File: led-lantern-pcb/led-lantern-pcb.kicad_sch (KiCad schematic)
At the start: 1 part, among them U1 TP4056

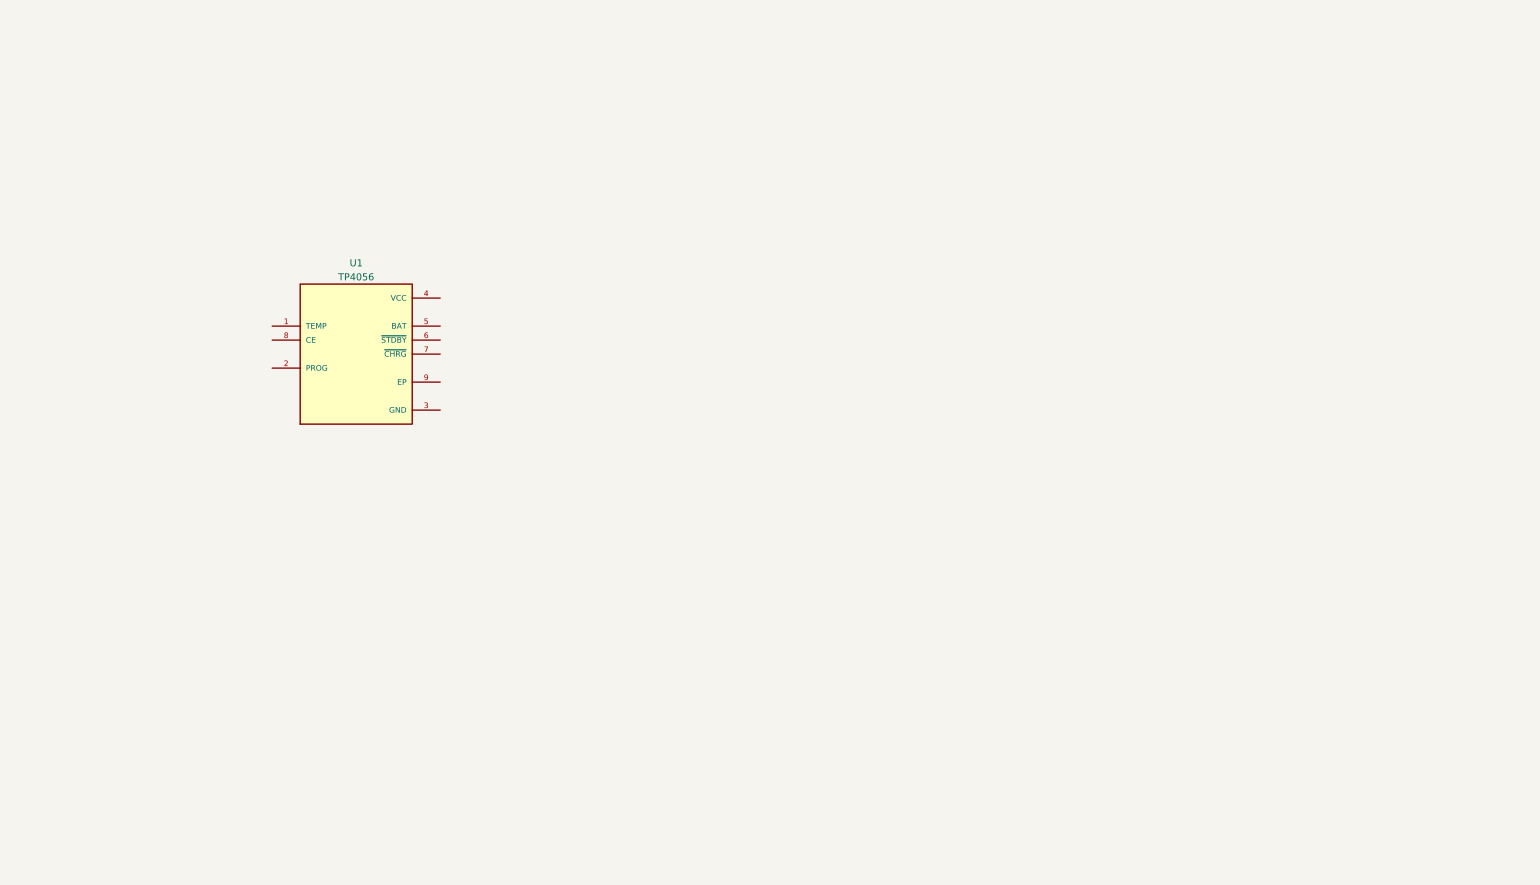
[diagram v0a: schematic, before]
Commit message: TP4056 and USB C (power only). Started on the DW01A circuit
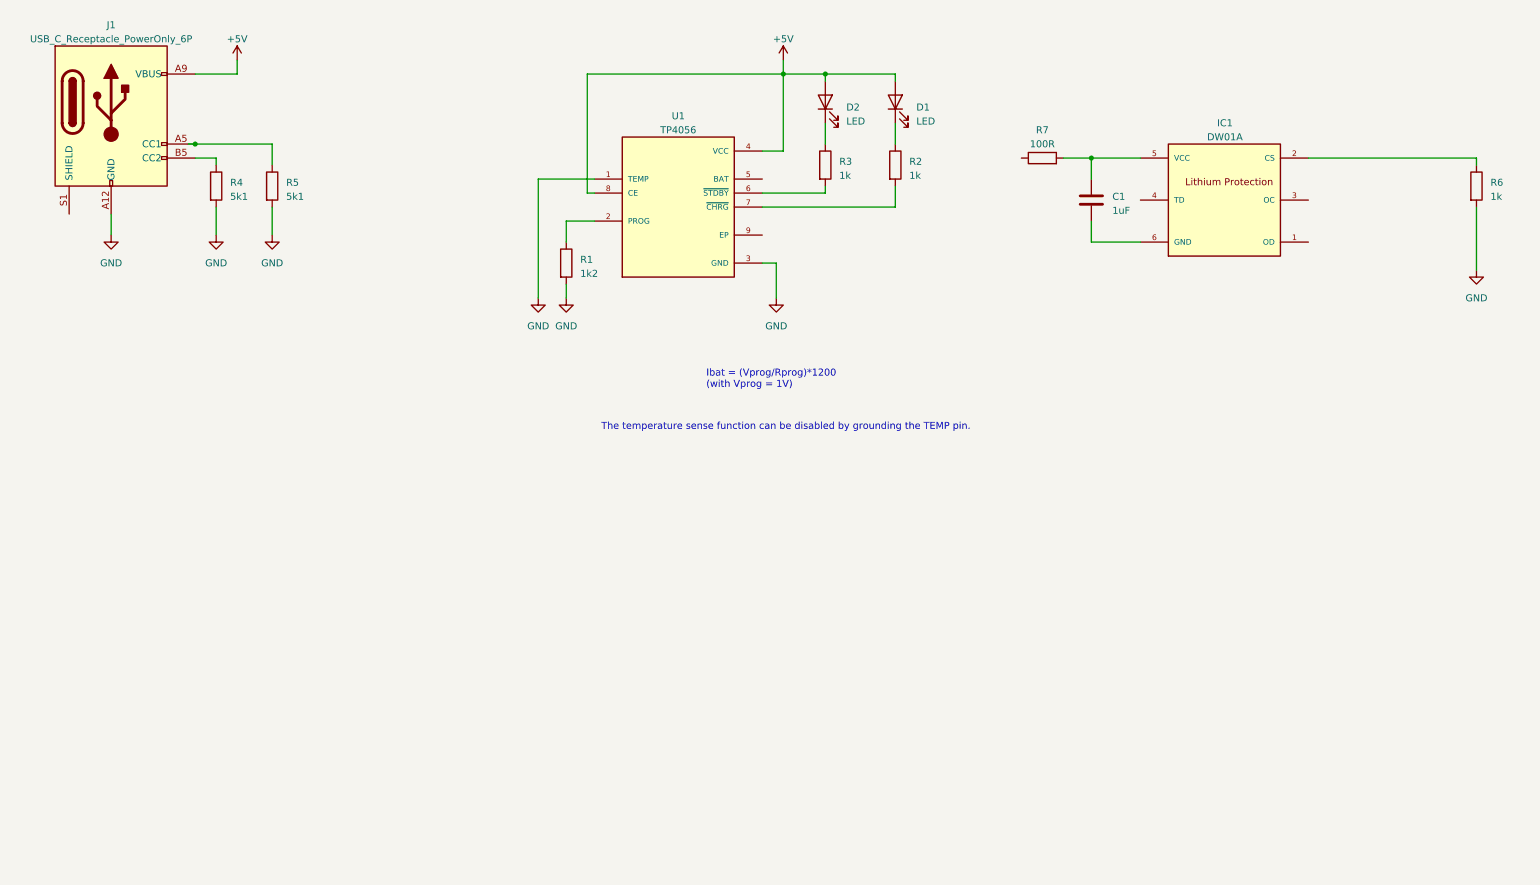
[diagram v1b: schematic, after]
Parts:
- added C1: 1uF, Resistor_SMD:R_0603_1608Metric_Pad0.98x0.95mm_HandSolder, symbol Device:C
- added D1, D2: LED, LED_SMD:LED_0603_1608Metric_Pad1.05x0.95mm_HandSolder, symbol Device:LED
- added IC1: DW01A, SOT23-6, symbol justin-library:DW01A
- added J1: USB_C_Receptacle_PowerOnly_6P, Connector_USB:USB_C_Receptacle_GCT_USB4135-GF-A_6P_TopMnt_Horizontal, symbol Connector:USB_C_Receptacle_PowerOnly_6P
- added R1: 1k2, Resistor_SMD:R_0603_1608Metric_Pad0.98x0.95mm_HandSolder, symbol Device:R
- added R2, R3, R6: 1k, Resistor_SMD:R_0603_1608Metric_Pad0.98x0.95mm_HandSolder, symbol Device:R
- added R4, R5: 5k1, Resistor_SMD:R_0201_0603Metric_Pad0.64x0.40mm_HandSolder, symbol Device:R
- added R7: 100R, Resistor_SMD:R_0603_1608Metric_Pad0.98x0.95mm_HandSolder, symbol Device:R
- U1: footprint SOP127P600X175-9N -> justin-library:SOP127P600X175-9N; lcsc (none) -> C725790
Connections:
- net GND: now reaches U1.1 (TEMP)
- net GND: now also U1.3 (GND), J1.A12 (GND), J1.B12 (GND), R1.2, R4.2, R5.2, R6.2
- net at U1.2 (PROG): now also R1.1
- net +5V: now reaches U1.4 (VCC)
- net +5V: now also U1.8 (CE), D1.2 (A), D2.2 (A), J1.A9 (VBUS), J1.B9 (VBUS)
- net at U1.6 (~{STDBY}): now also R3.2
- net at U1.7 (~{CHRG}): now also R2.2
- new net: J1.A5 (CC1), R5.1
- new net: J1.B5 (CC2), R4.1
- new net: D2.1 (K), R3.1
- new net: IC1.2 (CS), R6.1
- new net: C1.1, IC1.5 (VCC), R7.2
- new net: C1.2, IC1.6 (GND)
- new net: D1.1 (K), R2.1
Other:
- note added: "Ibat = (Vprog/Rprog)*1200 (with Vprog = 1V)"
- note added: "The temperature sense function can be disabled by grounding the TEMP pin."
- moved on the sheet: U1

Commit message: schematic into blocks and added auto power path control to schematic
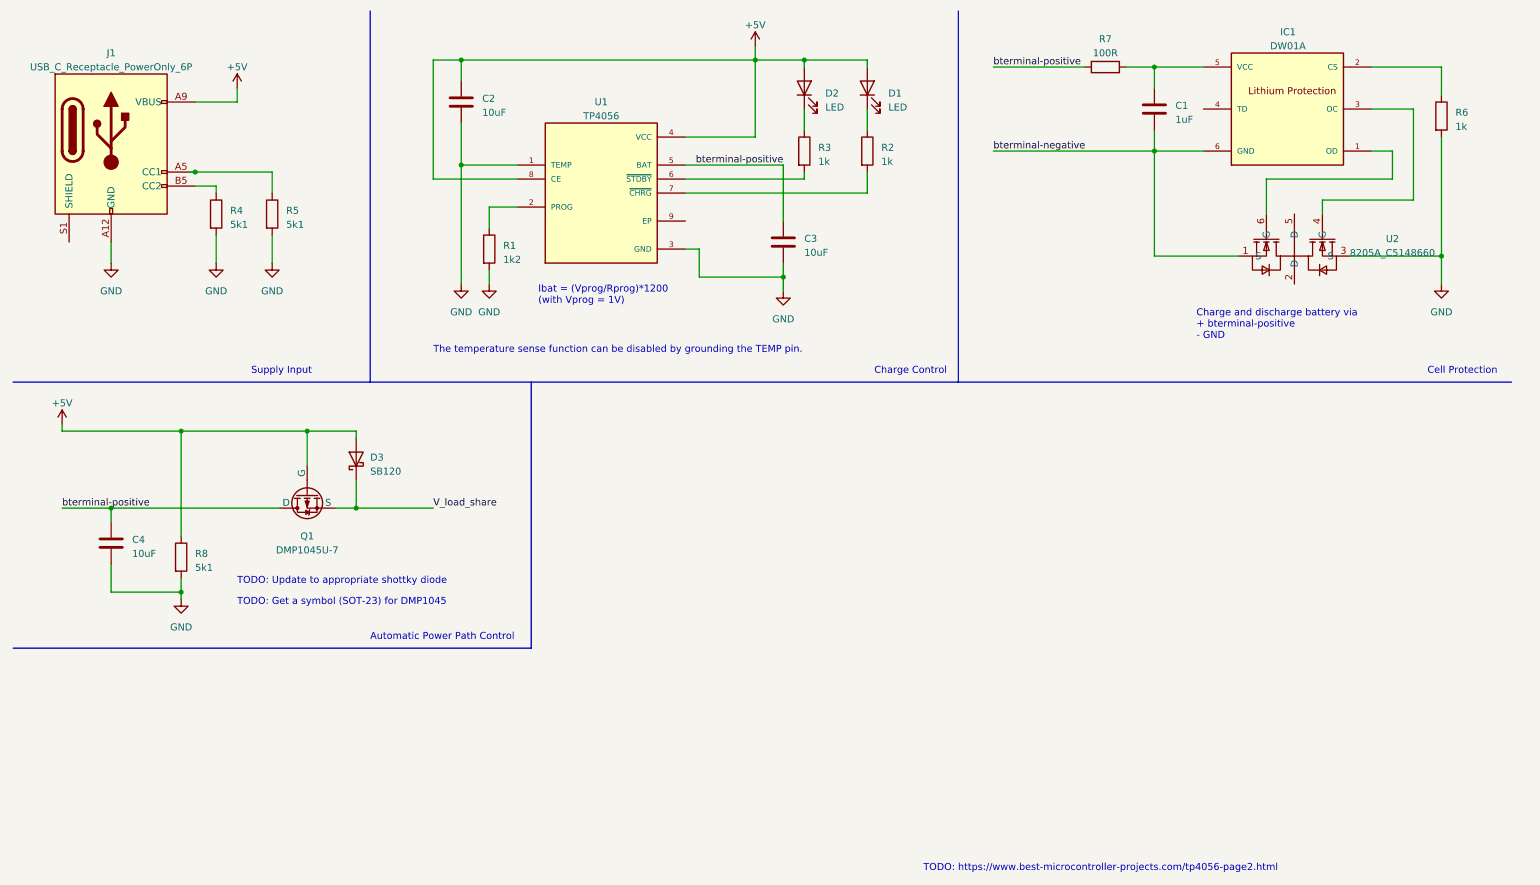
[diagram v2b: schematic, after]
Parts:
- added C2, C3, C4: 10uF, Capacitor_SMD:C_0603_1608Metric_Pad1.08x0.95mm_HandSolder, symbol Device:C
- added D3: SB120, Diode_THT:D_DO-41_SOD81_P10.16mm_Horizontal, symbol Diode:SB120
- added Q1: DMP1045U-7, symbol justin-library:DMP1045U-7
- added R8: 5k1, Resistor_SMD:R_0201_0603Metric_Pad0.64x0.40mm_HandSolder, symbol Device:R
- added U2: 8205A_C5148660, easyeda2kicad:SOT-23-6_L2.9-W1.6-P0.95-LS2.8-BR, symbol justin-library:8205A_C5148660
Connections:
- net +5V: now also C2.1, D3.2 (A), Q1.2 (G), R8.1
- net GND: now also C2.2, C3.2, C4.2, R8.2, U2.3 (S)
- net at IC1.1 (OD): now also U2.6 (G)
- net at IC1.3 (OC): now also U2.4 (G)
- net bterminal-negative: now reaches C1.2, IC1.6 (GND)
- net bterminal-negative: now also U2.1 (S)
- net bterminal-positive: now reaches R7.1
- net bterminal-positive: now also U1.5 (BAT), C3.1, C4.1, Q1.1 (D)
- new net V_load_share: D3.1 (K), Q1.3 (S)
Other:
- note added: "Automatic Power Path Control"
- note added: "Cell Protection"
- note added: "Charge Control"
- note added: "Charge and discharge battery via + bterminal-positive - GND"
- note added: "Supply Input"
- note added: "TODO: Get a symbol (SOT-23) for DMP1045"
- note added: "TODO: Update to appropriate shottky diode"
- note added: "TODO: https://www.best-microcontroller-projects.com/tp4056-page2.html"
- moved on the sheet: C1, D1, D2, IC1, J1, R1, R2, R3, R4, R5, R6, R7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
